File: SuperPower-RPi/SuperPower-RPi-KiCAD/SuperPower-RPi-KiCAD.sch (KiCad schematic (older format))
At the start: 4 parts

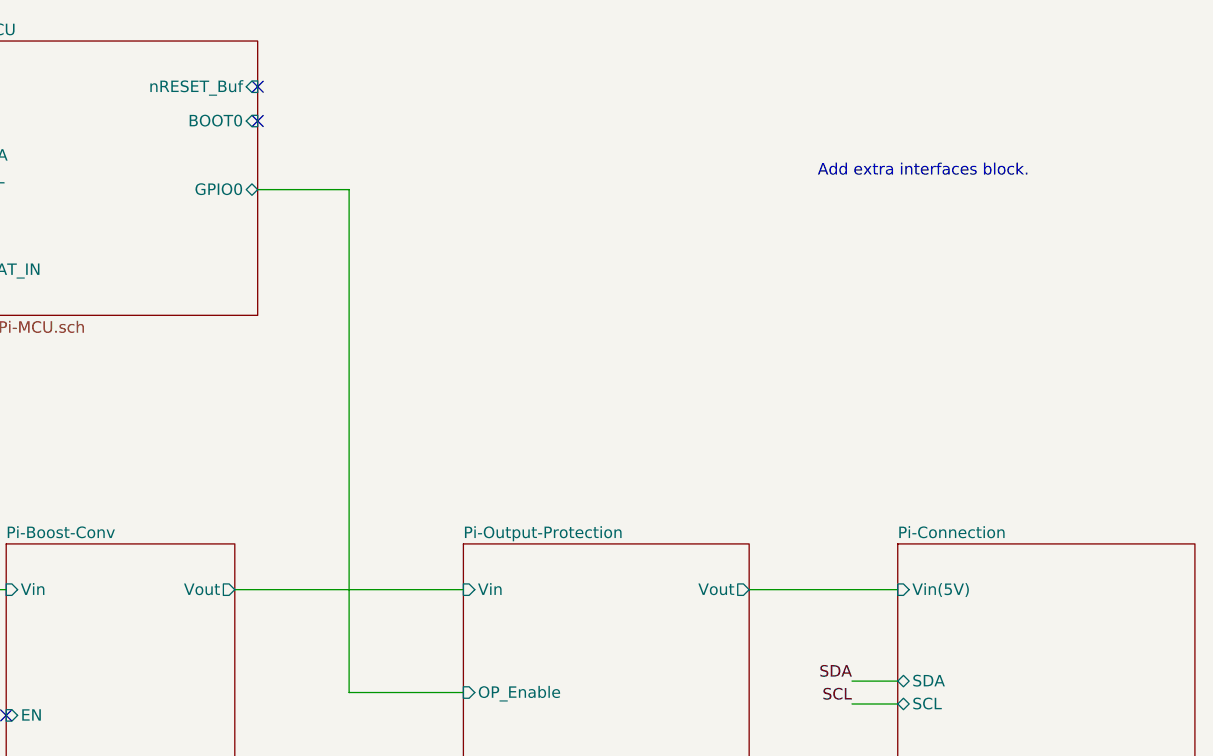
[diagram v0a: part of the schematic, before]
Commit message: Added voltage divider to measure 5V rail.
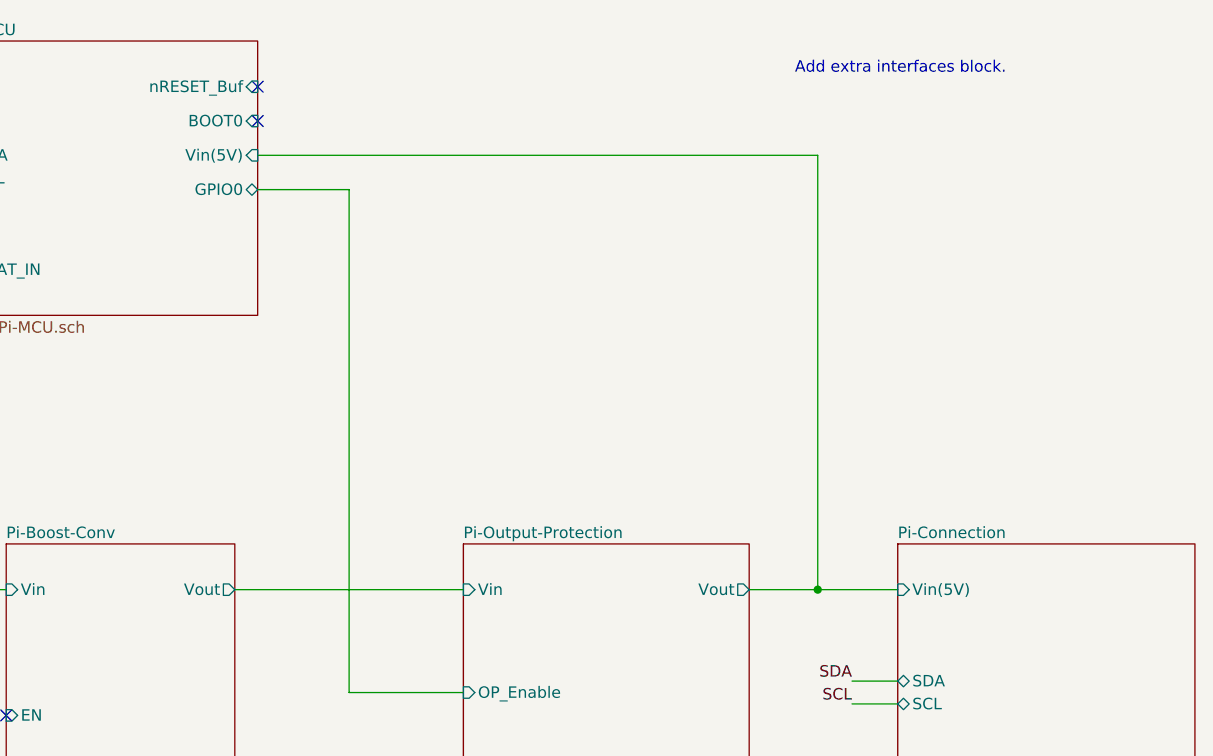
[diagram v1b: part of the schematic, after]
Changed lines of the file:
@@
 	3200 4400 2950 4400
 Wire Wire Line
-	8700 3650 9350 3650
+	8700 3650 9000 3650
 Wire Wire Line
 	6450 3650 7450 3650
@@
 $EndSheet
 $Sheet
-S 5250 1250 1300 1200
-U 5F6AC872
-F0 "Pi-MCU" 50
-F1 "Pi-MCU.sch" 50
-F2 "SDA" B L 5250 1750 50
-F3 "SCL" B L 5250 1850 50
-F4 "GPIO0" B R 6550 1900 50
-F5 "VBAT_IN" I L 5250 2250 50
-F6 "nRESET_Buf" I R 6550 1450 50
-F7 "BOOT0" I R 6550 1600 50
-$EndSheet
-$Sheet
 S 3200 5350 1250 1050
 U 5F6AC644
@@
 Wire Wire Line
 	3200 4050 2300 4050
-Text Notes 9000 1850 0    50   ~ 0
+Text Notes 8900 1400 0    50   ~ 0
 Add extra interfaces block.
 Wire Wire Line
@@
 NoConn ~ 6550 1450
 NoConn ~ 6550 1600
+$Sheet
+S 5250 1250 1300 1200
+U 5F6AC872
+F0 "Pi-MCU" 50
+F1 "Pi-MCU.sch" 50
+F2 "SDA" B L 5250 1750 50
+F3 "SCL" B L 5250 1850 50
+F4 "GPIO0" B R 6550 1900 50
+F5 "VBAT_IN" I L 5250 2250 50
+F6 "nRESET_Buf" I R 6550 1450 50
+F7 "BOOT0" I R 6550 1600 50
+F8 "Vin(5V)" I R 6550 1750 50
+$EndSheet
+Wire Wire Line
+	6550 1750 9000 1750
+Wire Wire Line
+	9000 1750 9000 3650
+Connection ~ 9000 3650
+Wire Wire Line
+	9000 3650 9350 3650
 $EndSCHEMATC

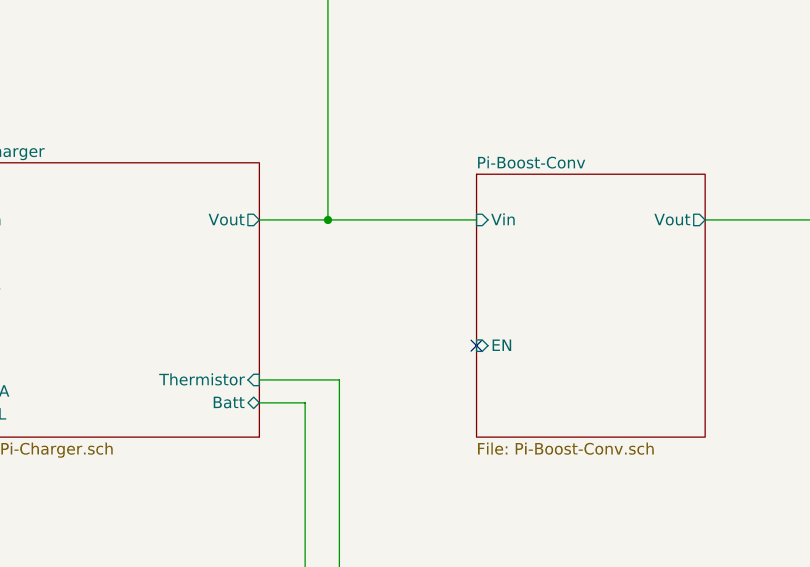
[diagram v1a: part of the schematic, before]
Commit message: Added Thermistor voltage divider and jumper on CE.
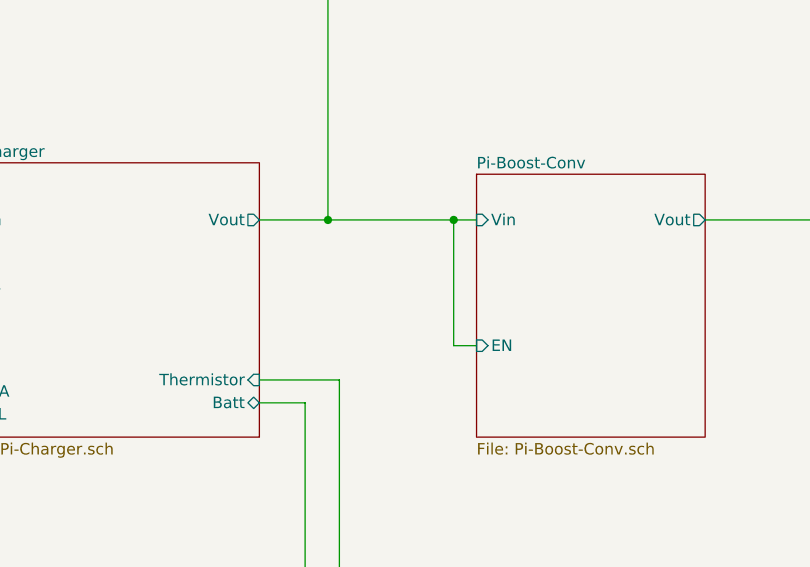
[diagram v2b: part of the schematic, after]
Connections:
- no-connect marks 3 -> 2
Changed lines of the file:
@@
 F9 "D-" I L 3200 4050 50
 $EndSheet
-NoConn ~ 5450 4200
 Wire Wire Line
 	4450 5600 4850 5600
@@
 Connection ~ 4800 3650
 Wire Wire Line
-	4800 3650 5450 3650
+	4800 3650 5350 3650
 Wire Wire Line
 	4800 2250 4800 3650
@@
 Wire Wire Line
 	9000 3650 9350 3650
+Wire Wire Line
+	5450 4200 5350 4200
+Wire Wire Line
+	5350 4200 5350 3650
+Connection ~ 5350 3650
+Wire Wire Line
+	5350 3650 5450 3650
 $EndSCHEMATC

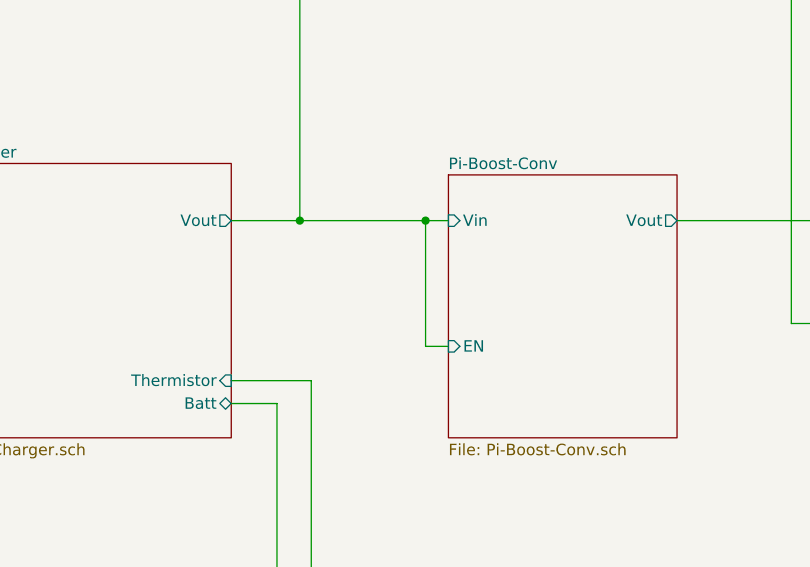
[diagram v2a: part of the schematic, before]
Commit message: Added DotStar to MCU page, and a jumper to Boost converter Enable pin.
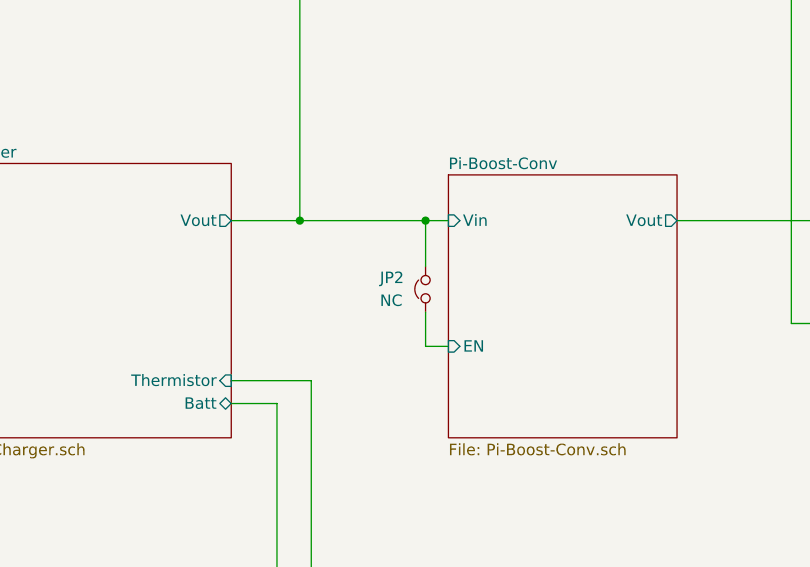
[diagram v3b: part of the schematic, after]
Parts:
- added JP2: NC, Jumper:SolderJumper-2_P1.3mm_Bridged_Pad1.0x1.5mm, symbol Device:Jumper_NC_Small
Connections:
- net Pi-Boost-Conv/EN: now also JP2.1
- new net Pi-Boost-Conv/Vin: JP2.2
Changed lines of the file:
@@
 Connection ~ 4800 3650
-Wire Wire Line
-	4800 3650 5350 3650
 Wire Wire Line
 	4800 2250 4800 3650
@@
 Wire Wire Line
 	5450 4200 5350 4200
+$Comp
+L Device:Jumper_NC_Small JP?
+U 1 1 5FBAF3BD
+P 5350 3950
+AR Path="/5F6AC481/5FBAF3BD" Ref="JP?"  Part="1"
+AR Path="/5FBAF3BD" Ref="JP2"  Part="1"
+F 0 "JP2" V 5400 4150 50  0000 R CNN
+F 1 "NC" V 5300 4150 50  0000 R CNN
+F 2 "Jumper:SolderJumper-2_P1.3mm_Bridged_Pad1.0x1.5mm" H 5350 3950 50  0001 C CNN
+F 3 "~" H 5350 3950 50  0001 C CNN
+	1    5350 3950
+	0    -1   -1   0
+$EndComp
 Wire Wire Line
-	5350 4200 5350 3650
+	5350 3650 5450 3650
+Wire Wire Line
+	4800 3650 5350 3650
 Connection ~ 5350 3650
 Wire Wire Line
-	5350 3650 5450 3650
+	5350 4200 5350 4050
+Wire Wire Line
+	5350 3850 5350 3650
 $EndSCHEMATC

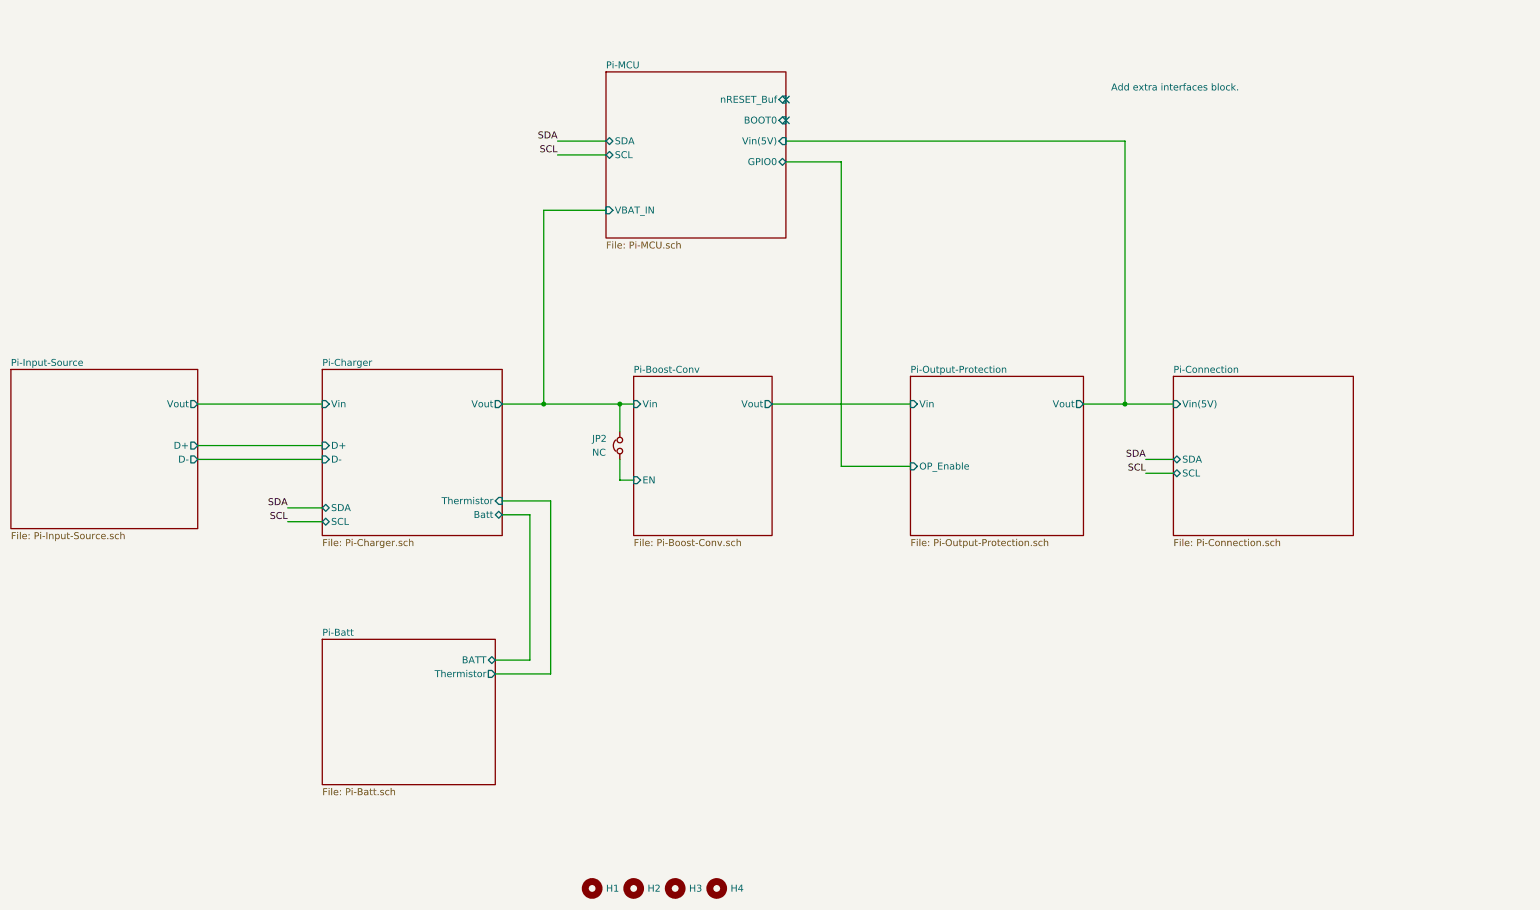
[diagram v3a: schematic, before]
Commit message: Added TODO notes from today's meeting and added some items on MCU sheet.
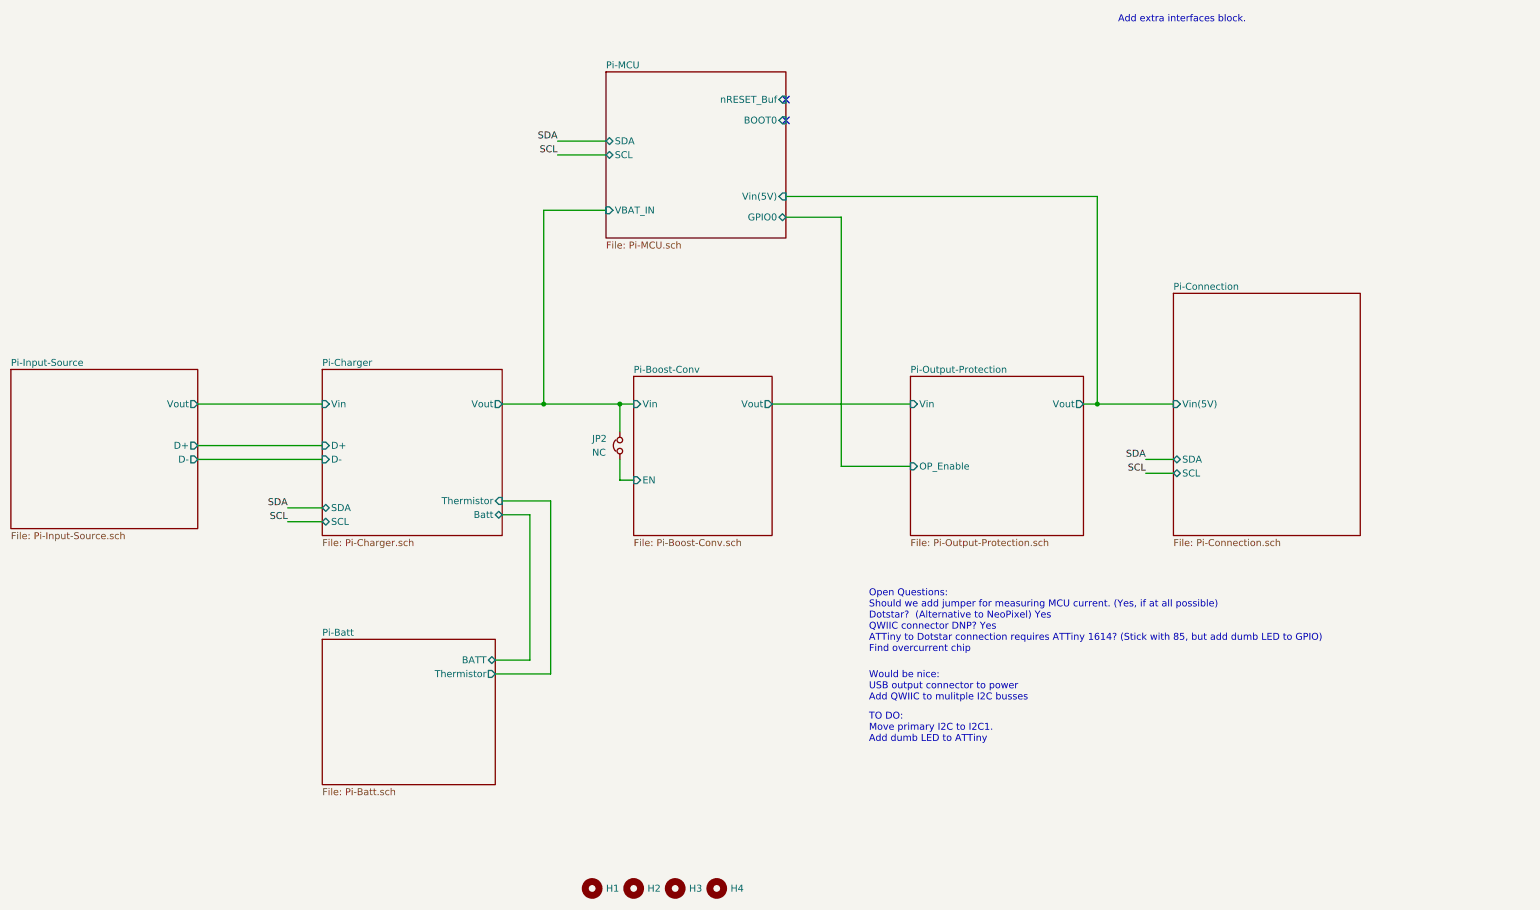
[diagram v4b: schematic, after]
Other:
- note added: "Open Questions:\nShould we add jumper for measuring MCU current. (Yes, if at all possible)\nDotstar? (Alternative to NeoPixel) Yes\nQWIIC connector DNP? Yes\nATTiny to Dotstar connection requires ATTiny 1614? (Stick with 85, but add dumb LED to GPIO)\nFind overcurrent chip"
- note added: "TO DO:\nMove primary I2C to I2C1.\nAdd dumb LED to ATTiny"
- note added: "Would be nice:\nUSB output connector to power \nAdd QWIIC to mulitple I2C busses\n"
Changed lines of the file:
@@
 	6950 4100 7450 4100
 Wire Wire Line
-	6950 1900 6950 4100
-Wire Wire Line
-	6550 1900 6950 1900
+	6550 2300 6950 2300
 Wire Wire Line
 	9150 4150 9350 4150
@@
 	3200 4400 2950 4400
 Wire Wire Line
-	8700 3650 9000 3650
+	8700 3650 8800 3650
 Wire Wire Line
 	6450 3650 7450 3650
@@
 F3 "Vout" O R 8700 3650 50
 F4 "OP_Enable" I L 7450 4100 50
-$EndSheet
-$Sheet
-S 9350 3450 1300 1150
-U 5F6AC9CB
-F0 "Pi-Connection" 50
-F1 "Pi-Connection.sch" 50
-F2 "Vin(5V)" I L 9350 3650 50
-F3 "SDA" B L 9350 4050 50
-F4 "SCL" B L 9350 4150 50
 $EndSheet
 $Sheet
@@
 Wire Wire Line
 	3200 4050 2300 4050
-Text Notes 8900 1400 0    50   ~ 0
+Text Notes 8950 900  0    50   ~ 0
 Add extra interfaces block.
 Wire Wire Line
@@
 F2 "SDA" B L 5250 1750 50
 F3 "SCL" B L 5250 1850 50
-F4 "GPIO0" B R 6550 1900 50
+F4 "GPIO0" B R 6550 2300 50
 F5 "VBAT_IN" I L 5250 2250 50
 F6 "nRESET_Buf" I R 6550 1450 50
 F7 "BOOT0" I R 6550 1600 50
-F8 "Vin(5V)" I R 6550 1750 50
-$EndSheet
-Wire Wire Line
-	6550 1750 9000 1750
-Wire Wire Line
-	9000 1750 9000 3650
-Connection ~ 9000 3650
-Wire Wire Line
-	9000 3650 9350 3650
+F8 "Vin(5V)" I R 6550 2150 50
+$EndSheet
+Wire Wire Line
+	6550 2150 8800 2150
 Wire Wire Line
 	5450 4200 5350 4200
@@
 Wire Wire Line
 	5350 3850 5350 3650
+Wire Wire Line
+	6950 2300 6950 4100
+Wire Wire Line
+	8800 2150 8800 3650
+Text Notes 7150 5450 0    50   ~ 0
+Open Questions:\nShould we add jumper for measuring MCU current. (Yes, if at all possible)\nDotstar?  (Alternative to NeoPixel) Yes\nQWIIC connector DNP? Yes\nATTiny to Dotstar connection requires ATTiny 1614? (Stick with 85, but add dumb LED to GPIO)\nFind overcurrent chip
+$Sheet
+S 9350 2850 1350 1750
+U 5F6AC9CB
+F0 "Pi-Connection" 50
+F1 "Pi-Connection.sch" 50
+F2 "Vin(5V)" I L 9350 3650 50
+F3 "SDA" B L 9350 4050 50
+F4 "SCL" B L 9350 4150 50
+$EndSheet
+Connection ~ 8800 3650
+Wire Wire Line
+	8800 3650 9350 3650
+Text Notes 7150 5800 0    50   ~ 0
+Would be nice:\nUSB output connector to power \nAdd QWIIC to mulitple I2C busses\n
+Text Notes 7150 6100 0    50   ~ 0
+TO DO:\nMove primary I2C to I2C1.\nAdd dumb LED to ATTiny
 $EndSCHEMATC
